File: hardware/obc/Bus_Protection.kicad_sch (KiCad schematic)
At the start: 44 parts, among them Q201 BSS138DWQ-7, Q202 BSS138DWQ-7, Q203 MBT2222ADW1T1, Q204 MBT2222ADW1T1, Q205 BSS138DWQ-7, Q206 BSS138DWQ-7, Q207 MBT2222ADW1T1, Q208 MBT2222ADW1T1, Q209 MMDT2907

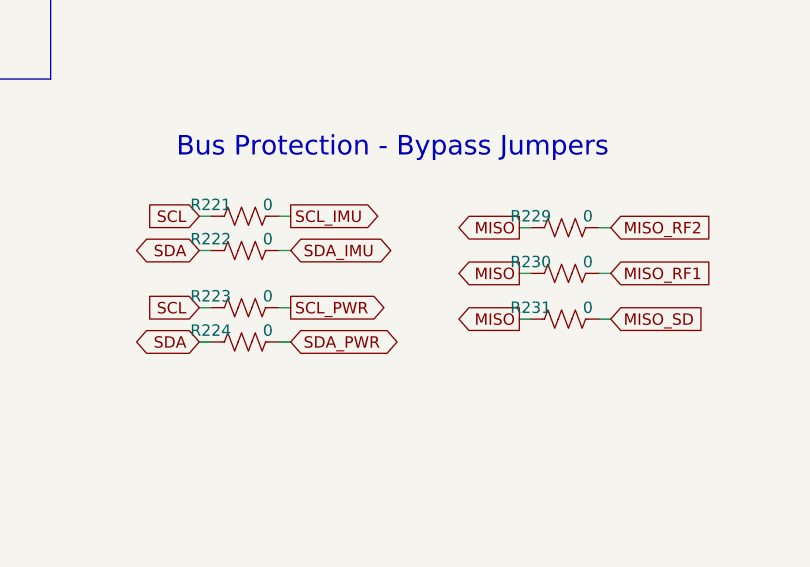
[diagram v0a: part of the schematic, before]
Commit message: obc: begun formal layout
Organized the components of the first two schematic pages into formal layout and switched out connector components. Introduced step files for previously developed footprints.
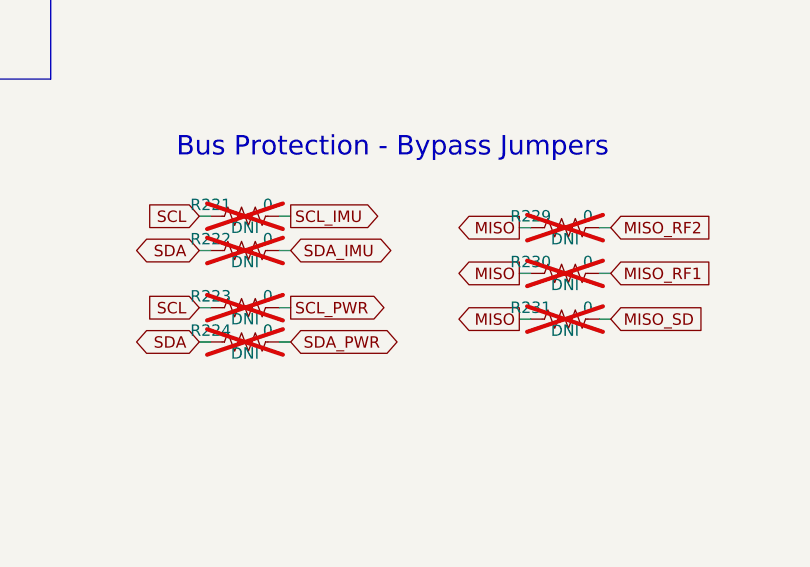
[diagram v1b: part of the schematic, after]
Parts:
- R221, R222, R223, R224, R229, R230, R231: DNI (none) -> DNI; now not fitted
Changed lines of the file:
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@@
 		(in_bom yes)
 		(on_board yes)
-		(dnp no)
+		(dnp yes)
 		(property "Reference" "R224"
 			(at 195.58 106.68 90)
@@
 			)
 		)
-		(property "DNI" ""
+		(property "DNI" "DNI"
 			(at 199.39 109.22 90)
 			(effects
@@
 		(in_bom yes)
 		(on_board yes)
-		(dnp no)
+		(dnp yes)
 		(property "Reference" "R221"
 			(at 195.58 92.71 90)
@@
 			)
 		)
-		(property "DNI" ""
+		(property "DNI" "DNI"
 			(at 199.39 95.25 90)
 			(effects
@@
 		(in_bom yes)
 		(on_board yes)
-		(dnp no)
+		(dnp yes)
 		(property "Reference" "R222"
 			(at 195.58 96.52 90)
@@
 			)
 		)
-		(property "DNI" ""
+		(property "DNI" "DNI"
 			(at 199.39 99.06 90)
 			(effects
@@
 		(in_bom yes)
 		(on_board yes)
-		(dnp no)
+		(dnp yes)
 		(property "Reference" "R230"
 			(at 231.14 99.06 90)
@@
 			)
 		)
-		(property "DNI" ""
+		(property "DNI" "DNI"
 			(at 234.95 101.6 90)
 			(effects
@@
 		(in_bom yes)
 		(on_board yes)
-		(dnp no)
+		(dnp yes)
 		(property "Reference" "R231"
 			(at 231.14 104.14 90)
@@
 			)
 		)
-		(property "DNI" ""
+		(property "DNI" "DNI"
 			(at 234.95 106.68 90)
 			(effects
@@
 		(in_bom yes)
 		(on_board yes)
-		(dnp no)
+		(dnp yes)
 		(property "Reference" "R223"
 			(at 195.58 102.87 90)
@@
 			)
 		)
-		(property "DNI" ""
+		(property "DNI" "DNI"
 			(at 199.39 105.41 90)
 			(effects
@@
 		(in_bom yes)
 		(on_board yes)
-		(dnp no)
+		(dnp yes)
 		(property "Reference" "R229"
 			(at 231.14 93.98 90)
@@
 			)
 		)
-		(property "DNI" ""
+		(property "DNI" "DNI"
 			(at 234.95 96.52 90)
 			(effects

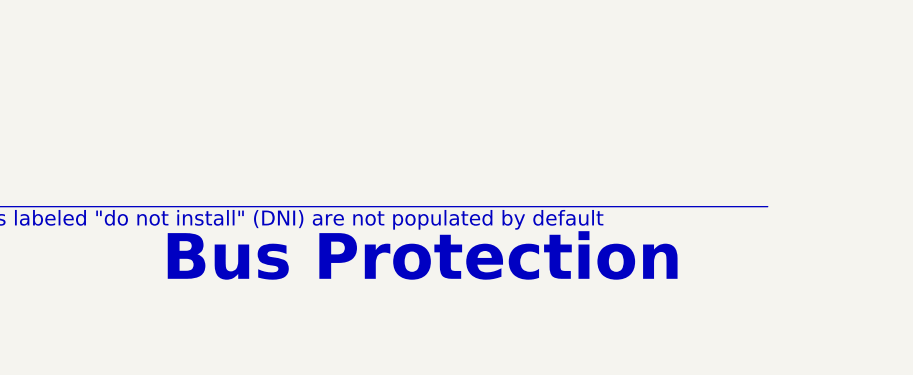
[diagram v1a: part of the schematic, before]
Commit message: obc: power connection cleanup
Decreased track length to vias and centered all vias in pad. Updated schematic title blocks, edited 3D models.
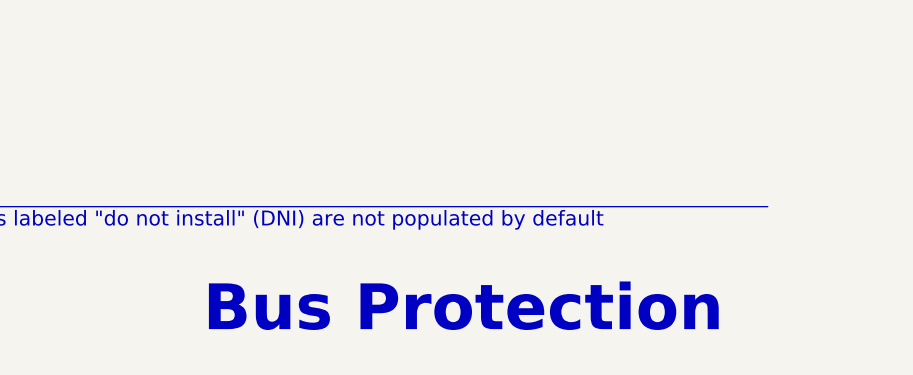
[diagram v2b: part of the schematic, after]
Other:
- company: Max Holliday -> Ruchir Kavulli, Michael Lyle
- title: PyCubed Mainboard -> Obi Wan Komputer
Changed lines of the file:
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@@
 	(paper "USLetter")
 	(title_block
-		(title "PyCubed Mainboard")
-		(date "2021-06-09")
-		(rev "v05c")
-		(company "Max Holliday")
+		(title "Obi Wan Komputer")
+		(date "2024-06-07")
+		(rev "vA")
+		(company "Ruchir Kavulli, Michael Lyle")
+		(comment 1 "Derived from PyCubed Mainboard v5")
 	)
 	(junction
@@
 	(text "Bus Protection"
 		(exclude_from_sim no)
-		(at 200.66 177.8 0)
+		(at 205.232 183.388 0)
 		(effects
 			(font

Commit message: obc: test traces for high priority signals
Preliminary trace creation for high priority signals.
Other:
- title: Obi Wan Komputer -> Obi Wan Computer
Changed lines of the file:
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@@
 	(paper "USLetter")
 	(title_block
-		(title "Obi Wan Komputer")
+		(title "Obi Wan Computer")
 		(date "2024-06-07")
 		(rev "vA")

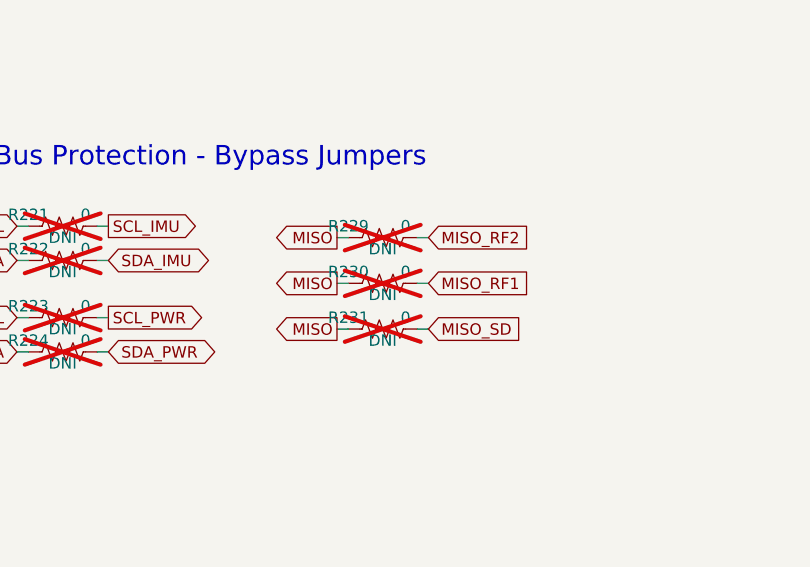
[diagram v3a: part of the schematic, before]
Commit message: obc: additional routing and placement edits
Routed ~70 more nets.
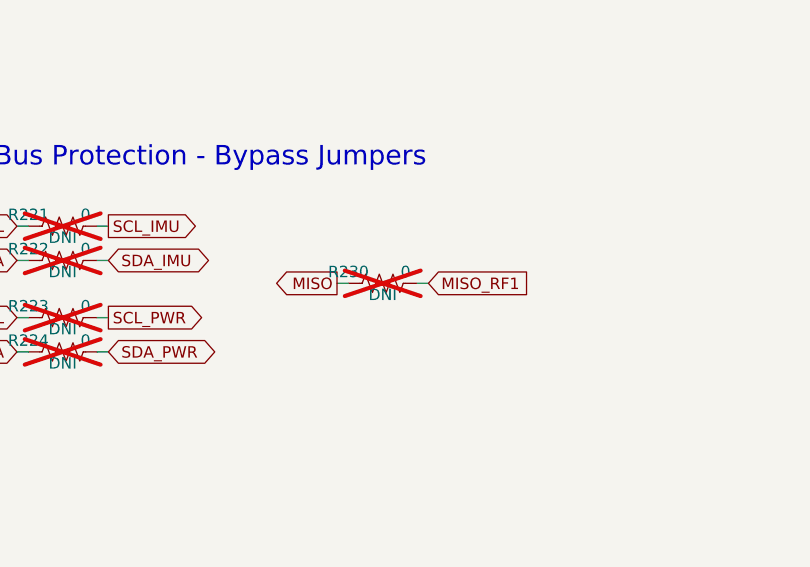
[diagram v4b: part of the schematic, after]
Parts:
- removed R229, R231: 0, Resistor_SMD:R_0603_1608Metric, symbol Device:R_US

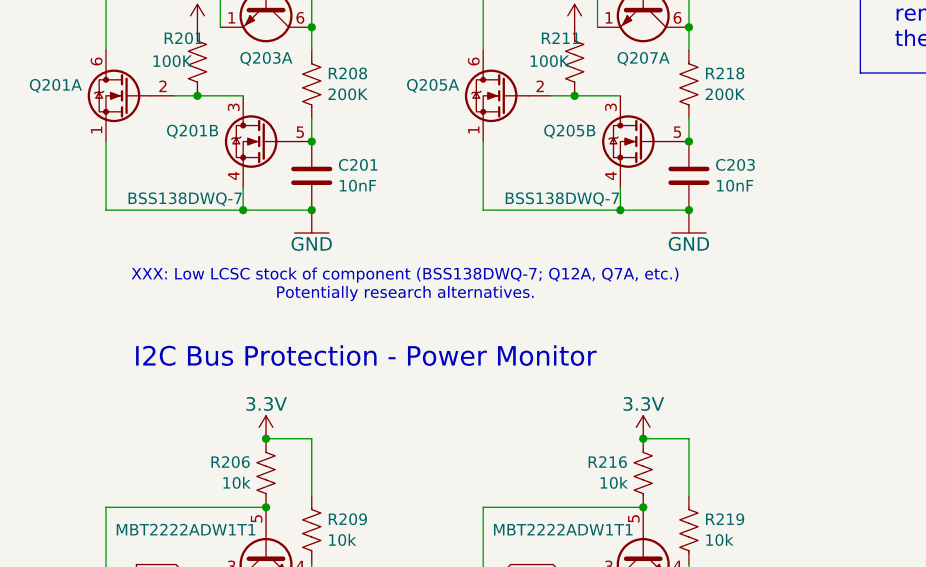
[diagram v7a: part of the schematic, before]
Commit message: obc: remove superfluous schem XXX comments
All were reviewed.

- Some didn't matter - entire comment removed
- Some were just notes, not action items - XXX notation removed

Two items noted do have implications, though:

- WDT rst pulldown value is incorrect.
- I2C pulls are missing (though this could be ignored).
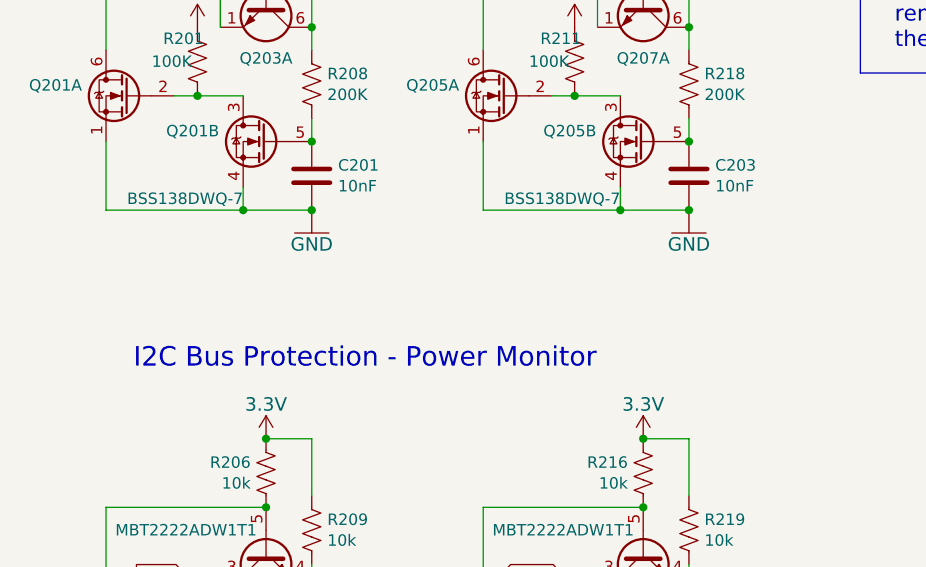
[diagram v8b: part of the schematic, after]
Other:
- note removed: "XXX: Low LCSC stock of component (BSS138DWQ-7; Q12A, Q7A, etc.) Potentially research alternatives."
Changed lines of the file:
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@@
-		)
-	)
-	(text "XXX: Low LCSC stock of component (BSS138DWQ-7; Q12A, Q7A, etc.)\nPotentially research alternatives.\n"
-		(exclude_from_sim no)
-		(at 61.214 102.362 0)
-		(effects
-			(font
-				(size 1.27 1.27)
-			)
 		)
 	)
